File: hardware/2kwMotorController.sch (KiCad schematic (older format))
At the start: 0 parts

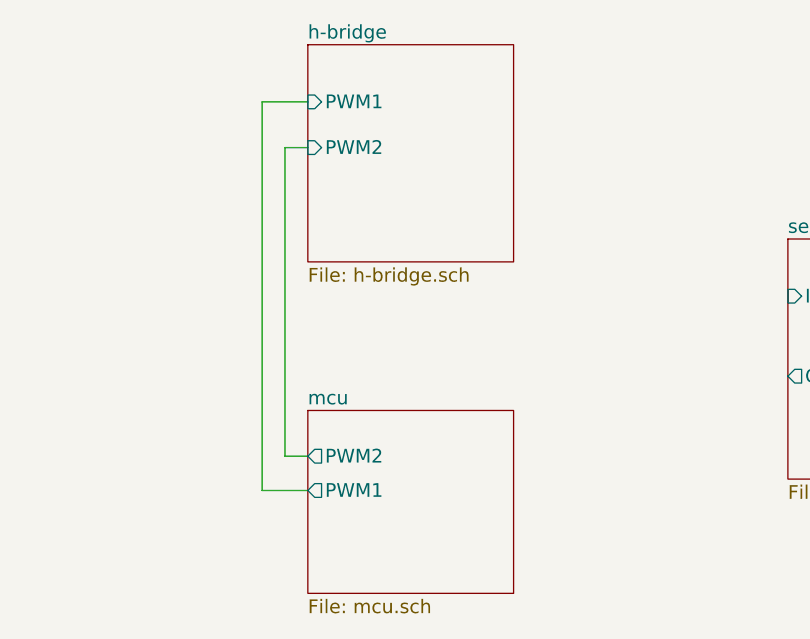
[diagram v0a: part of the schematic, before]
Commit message: cleaned up h-bridge; added digital isolators
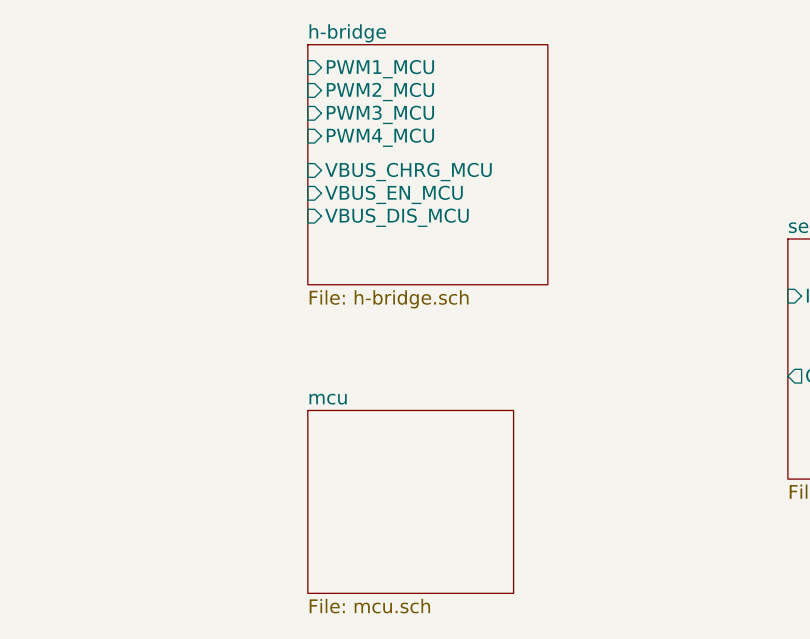
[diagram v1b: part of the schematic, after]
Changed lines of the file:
@@
 $EndDescr
 $Sheet
-S 5550 1950 900  950
+S 5550 1950 1050 1050
 U 5975734C
 F0 "h-bridge" 60
 F1 "h-bridge.sch" 60
-F2 "PWM1" I L 5550 2200 60
-F3 "PWM2" I L 5550 2400 60
+F2 "PWM1_MCU" I L 5550 2050 60
+F3 "PWM2_MCU" I L 5550 2150 60
+F4 "PWM3_MCU" I L 5550 2250 60
+F5 "PWM4_MCU" I L 5550 2350 60
+F6 "VBUS_CHRG_MCU" I L 5550 2500 60
+F7 "VBUS_EN_MCU" I L 5550 2600 60
+F8 "VBUS_DIS_MCU" I L 5550 2700 60
 $EndSheet
-$Sheet
-S 5550 3550 900  800
-U 59759ACE
-F0 "mcu" 60
-F1 "mcu.sch" 60
-F2 "PWM1" O L 5550 3900 60
-F3 "PWM2" O L 5550 3750 60
-$EndSheet
-Wire Wire Line
-	5550 2400 5450 2400
-Wire Wire Line
-	5450 2400 5450 3750
-Wire Wire Line
-	5450 3750 5550 3750
-Wire Wire Line
-	5550 3900 5350 3900
-Wire Wire Line
-	5350 3900 5350 2200
-Wire Wire Line
-	5350 2200 5550 2200
 $Sheet
 S 7650 2800 1200 1050
@@
 F1 "power.sch" 60
 $EndSheet
+$Sheet
+S 5550 3550 900  800
+U 59759ACE
+F0 "mcu" 60
+F1 "mcu.sch" 60
+$EndSheet
 $EndSCHEMATC

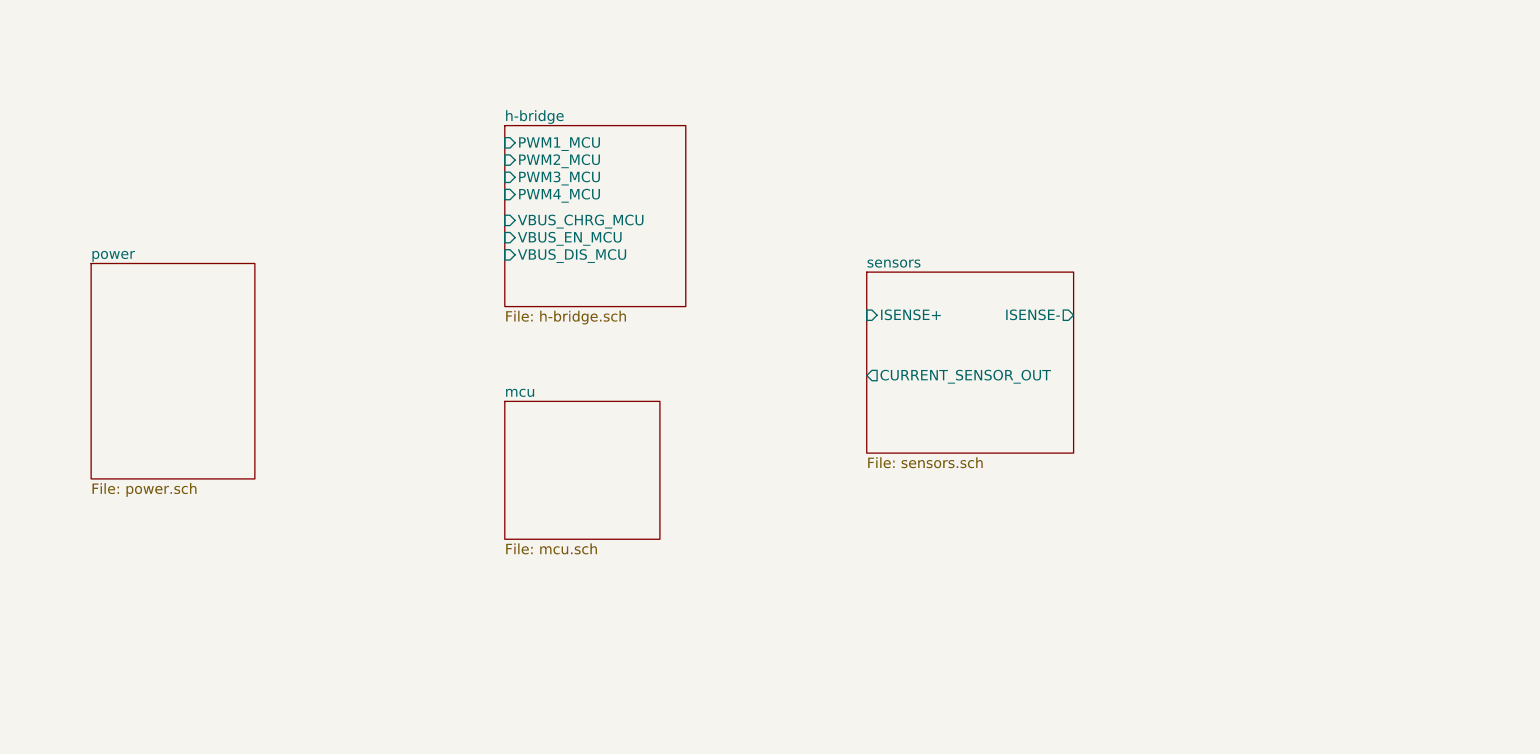
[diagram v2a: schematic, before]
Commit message: ERC cleanup, begin pcbnew population
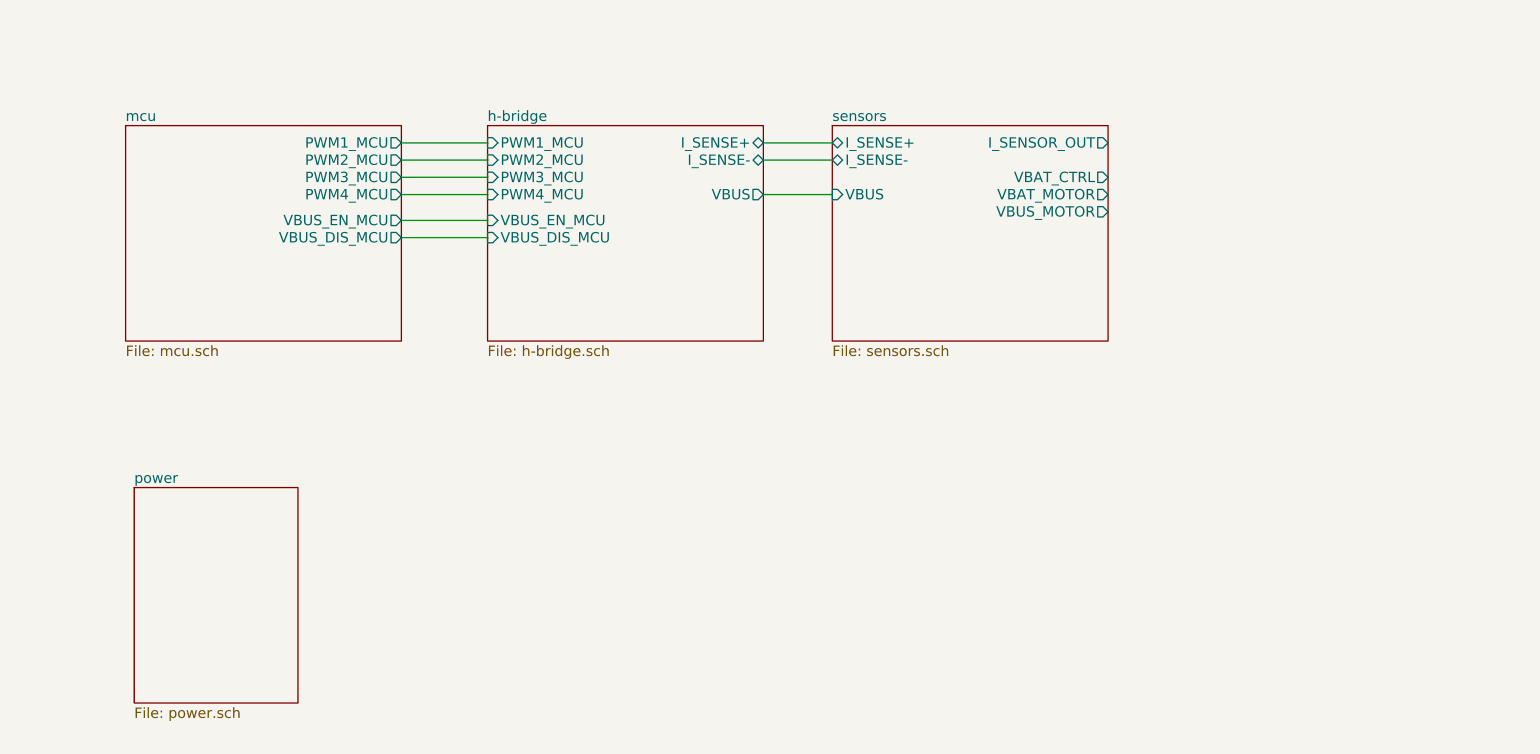
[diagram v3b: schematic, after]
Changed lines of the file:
@@
 $EndDescr
 $Sheet
-S 7650 2800 1200 1050
+S 7450 1950 1600 1250
 U 5975AD12
 F0 "sensors" 60
 F1 "sensors.sch" 60
-F2 "ISENSE+" I L 7650 3050 60
-F3 "ISENSE-" O R 8850 3050 60
-F4 "CURRENT_SENSOR_OUT" O L 7650 3400 60
+F2 "I_SENSE+" B L 7450 2050 60
+F3 "I_SENSE-" B L 7450 2150 60
+F4 "I_SENSOR_OUT" O R 9050 2050 60
+F5 "VBAT_CTRL" O R 9050 2250 60
+F6 "VBAT_MOTOR" O R 9050 2350 60
+F7 "VBUS_MOTOR" O R 9050 2450 60
+F8 "VBUS" I L 7450 2350 60
 $EndSheet
 $Sheet
-S 3150 2750 950  1250
+S 3400 4050 950  1250
 U 5975B0C1
 F0 "power" 60
@@
 $EndSheet
 $Sheet
-S 5550 3550 900  800
+S 3350 1950 1600 1250
 U 59759ACE
 F0 "mcu" 60
 F1 "mcu.sch" 60
+F2 "PWM1_MCU" O R 4950 2050 60
+F3 "PWM2_MCU" O R 4950 2150 60
+F4 "PWM3_MCU" O R 4950 2250 60
+F5 "PWM4_MCU" O R 4950 2350 60
+F6 "VBUS_EN_MCU" O R 4950 2500 60
+F7 "VBUS_DIS_MCU" O R 4950 2600 60
 $EndSheet
+Wire Wire Line
+	4950 2050 5450 2050
+Wire Wire Line
+	5450 2150 4950 2150
+Wire Wire Line
+	4950 2250 5450 2250
+Wire Wire Line
+	5450 2350 4950 2350
+Wire Wire Line
+	4950 2500 5450 2500
+Wire Wire Line
+	5450 2600 4950 2600
 $Sheet
-S 5550 1950 1050 1050
+S 5450 1950 1600 1250
 U 5975734C
 F0 "h-bridge" 60
 F1 "h-bridge.sch" 60
-F2 "PWM1_MCU" I L 5550 2050 60
-F3 "PWM2_MCU" I L 5550 2150 60
-F4 "PWM3_MCU" I L 5550 2250 60
-F5 "PWM4_MCU" I L 5550 2350 60
-F6 "VBUS_CHRG_MCU" I L 5550 2500 60
-F7 "VBUS_EN_MCU" I L 5550 2600 60
-F8 "VBUS_DIS_MCU" I L 5550 2700 60
+F2 "PWM1_MCU" I L 5450 2050 60
+F3 "PWM2_MCU" I L 5450 2150 60
+F4 "PWM3_MCU" I L 5450 2250 60
+F5 "PWM4_MCU" I L 5450 2350 60
+F6 "VBUS_EN_MCU" I L 5450 2500 60
+F7 "VBUS_DIS_MCU" I L 5450 2600 60
+F8 "I_SENSE+" B R 7050 2050 60
+F9 "I_SENSE-" B R 7050 2150 60
+F10 "VBUS" O R 7050 2350 60
 $EndSheet
+Wire Wire Line
+	7050 2050 7450 2050
+Wire Wire Line
+	7050 2150 7450 2150
+Wire Wire Line
+	7050 2350 7450 2350
 $EndSCHEMATC

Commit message: Finish MCU HW draft 1; adjust sensors for 3v ref
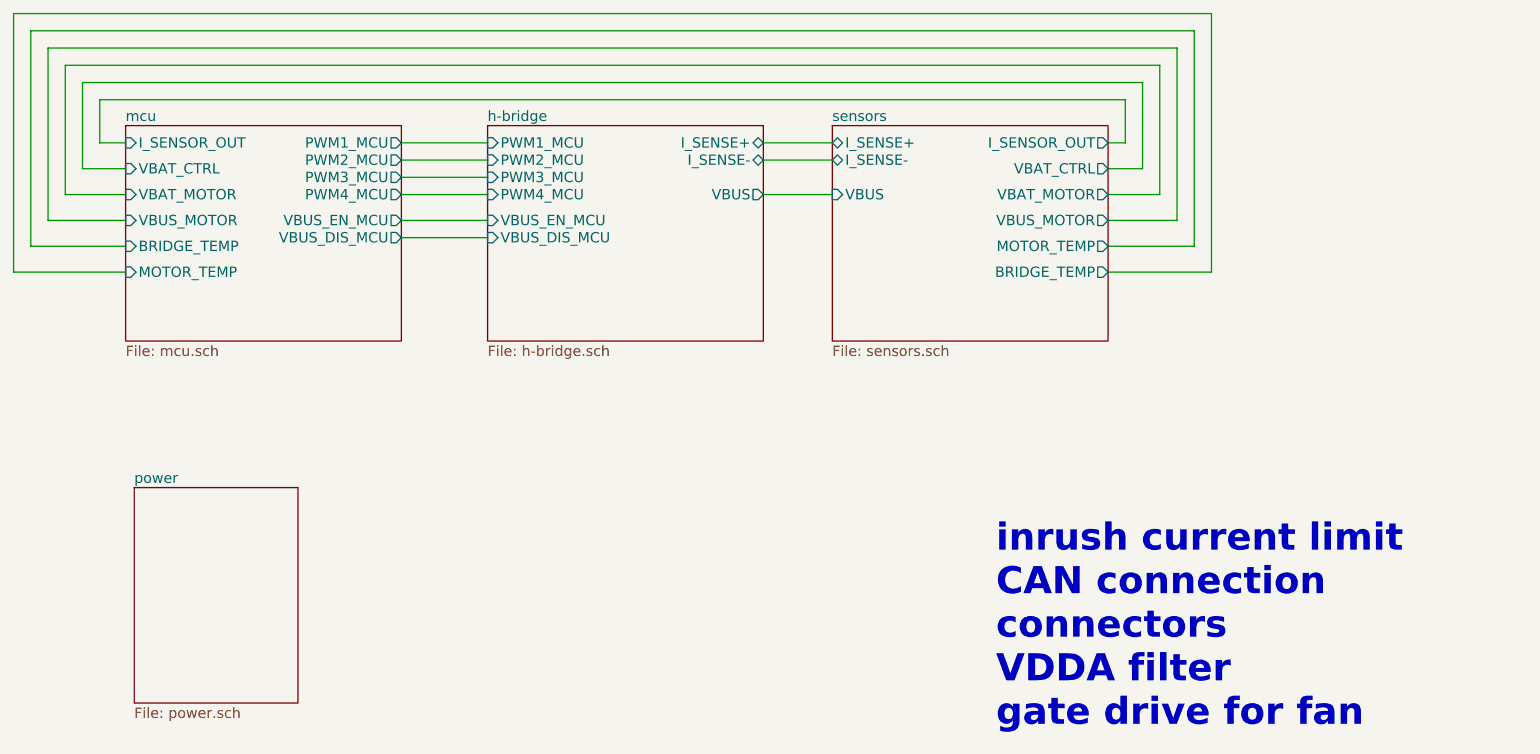
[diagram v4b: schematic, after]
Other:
- note added: "inrush current limit\nCAN connection\nconnectors\nVDDA filter\ngate drive for fan"
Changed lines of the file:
@@
 F3 "I_SENSE-" B L 7450 2150 60
 F4 "I_SENSOR_OUT" O R 9050 2050 60
-F5 "VBAT_CTRL" O R 9050 2250 60
+F5 "VBAT_CTRL" O R 9050 2200 60
 F6 "VBAT_MOTOR" O R 9050 2350 60
-F7 "VBUS_MOTOR" O R 9050 2450 60
+F7 "VBUS_MOTOR" O R 9050 2500 60
 F8 "VBUS" I L 7450 2350 60
+F9 "MOTOR_TEMP" O R 9050 2650 60
+F10 "BRIDGE_TEMP" O R 9050 2800 60
 $EndSheet
 $Sheet
@@
 F6 "VBUS_EN_MCU" O R 4950 2500 60
 F7 "VBUS_DIS_MCU" O R 4950 2600 60
+F8 "I_SENSOR_OUT" I L 3350 2050 60
+F9 "VBAT_CTRL" I L 3350 2200 60
+F10 "VBAT_MOTOR" I L 3350 2350 60
+F11 "VBUS_MOTOR" I L 3350 2500 60
+F12 "BRIDGE_TEMP" I L 3350 2650 60
+F13 "MOTOR_TEMP" I L 3350 2800 60
 $EndSheet
 Wire Wire Line
@@
 Wire Wire Line
 	7050 2350 7450 2350
+Wire Wire Line
+	9050 2050 9150 2050
+Wire Wire Line
+	9150 2050 9150 1800
+Wire Wire Line
+	9150 1800 3200 1800
+Wire Wire Line
+	9050 2200 9250 2200
+Wire Wire Line
+	9250 2200 9250 1700
+Wire Wire Line
+	9250 1700 3100 1700
+Wire Wire Line
+	3100 1700 3100 2200
+Wire Wire Line
+	3100 2200 3350 2200
+Wire Wire Line
+	3350 2050 3200 2050
+Wire Wire Line
+	3200 2050 3200 1800
+Wire Wire Line
+	3350 2350 3000 2350
+Wire Wire Line
+	3000 2350 3000 1600
+Wire Wire Line
+	3000 1600 9350 1600
+Wire Wire Line
+	9350 1600 9350 2350
+Wire Wire Line
+	9350 2350 9050 2350
+Wire Wire Line
+	9050 2500 9450 2500
+Wire Wire Line
+	9450 2500 9450 1500
+Wire Wire Line
+	9450 1500 2900 1500
+Wire Wire Line
+	2900 1500 2900 2500
+Wire Wire Line
+	2900 2500 3350 2500
+Wire Wire Line
+	3350 2650 2800 2650
+Wire Wire Line
+	2800 2650 2800 1400
+Wire Wire Line
+	2800 1400 9550 1400
+Wire Wire Line
+	9550 1400 9550 2650
+Wire Wire Line
+	9550 2650 9050 2650
+Wire Wire Line
+	9050 2800 9650 2800
+Wire Wire Line
+	9650 2800 9650 1300
+Wire Wire Line
+	9650 1300 2700 1300
+Wire Wire Line
+	2700 1300 2700 2800
+Wire Wire Line
+	2700 2800 3350 2800
+Text Notes 8400 5450 0    157  ~ 31
+inrush current limit\nCAN connection\nconnectors\nVDDA filter\ngate drive for fan
 $EndSCHEMATC

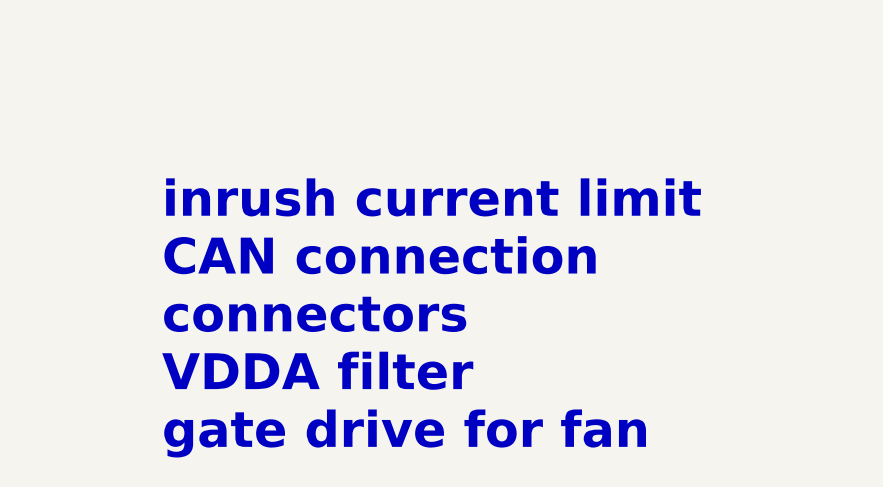
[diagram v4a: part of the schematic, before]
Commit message: Update sensors, hbridge caps, add heatsink
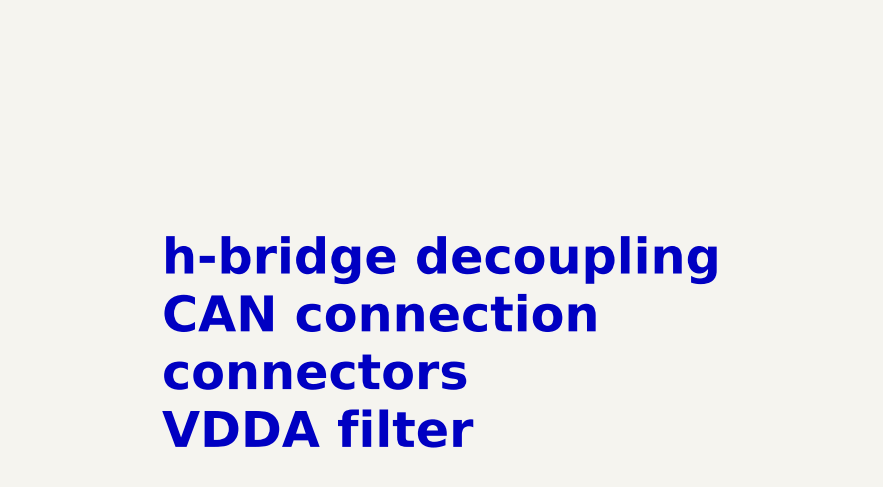
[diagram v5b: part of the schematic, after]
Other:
- note added: "h-bridge decoupling\nCAN connection\nconnectors\nVDDA filter"
- note removed: "inrush current limit\nCAN connection\nconnectors\nVDDA filter\ngate drive for fan"
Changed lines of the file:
@@
 	2700 2800 3350 2800
 Text Notes 8400 5450 0    157  ~ 31
-inrush current limit\nCAN connection\nconnectors\nVDDA filter\ngate drive for fan
+h-bridge decoupling\nCAN connection\nconnectors\nVDDA filter
 $EndSCHEMATC

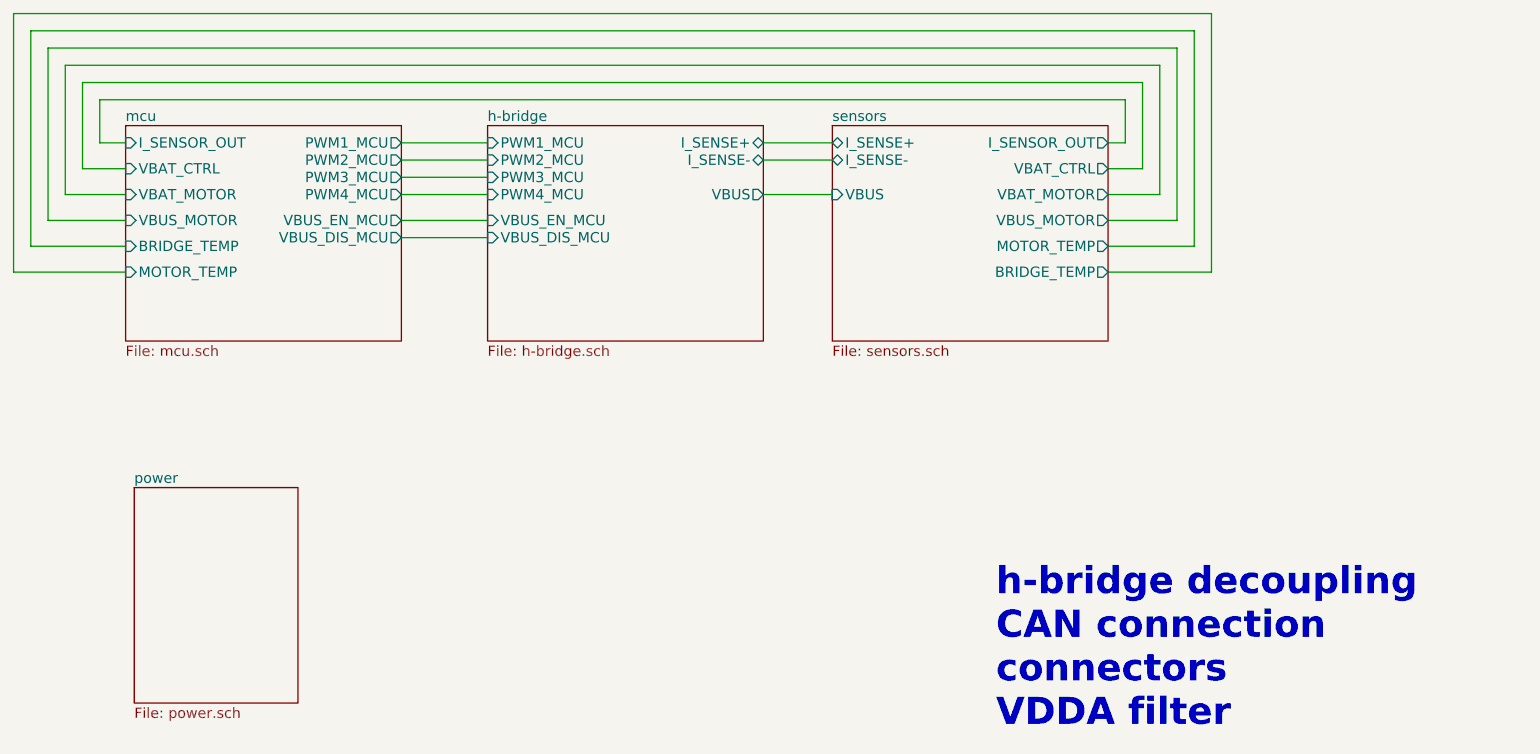
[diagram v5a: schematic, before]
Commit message: Draft layout of controller section
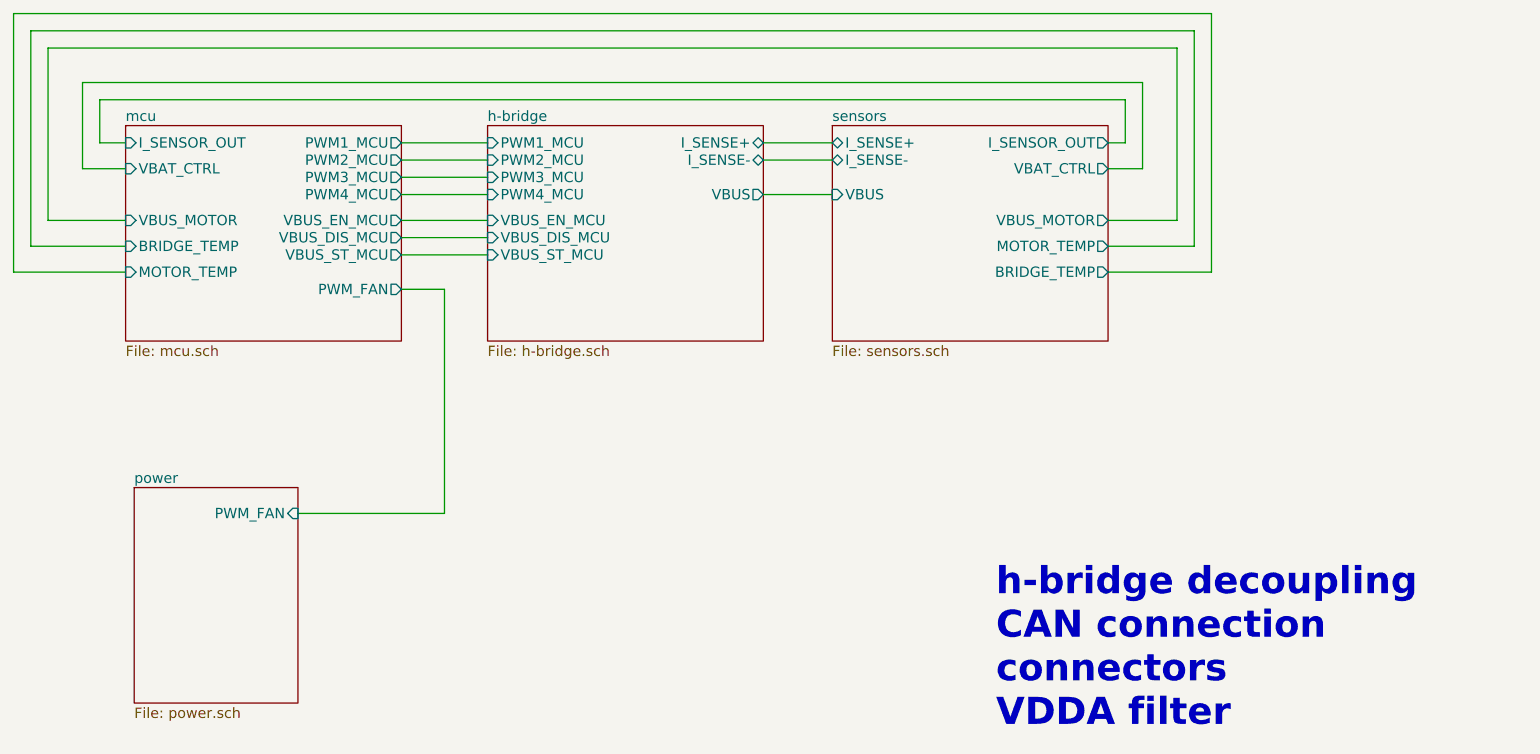
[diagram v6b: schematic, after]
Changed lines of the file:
@@
 F4 "I_SENSOR_OUT" O R 9050 2050 60
 F5 "VBAT_CTRL" O R 9050 2200 60
-F6 "VBAT_MOTOR" O R 9050 2350 60
-F7 "VBUS_MOTOR" O R 9050 2500 60
-F8 "VBUS" I L 7450 2350 60
-F9 "MOTOR_TEMP" O R 9050 2650 60
-F10 "BRIDGE_TEMP" O R 9050 2800 60
+F6 "VBUS_MOTOR" O R 9050 2500 60
+F7 "VBUS" I L 7450 2350 60
+F8 "MOTOR_TEMP" O R 9050 2650 60
+F9 "BRIDGE_TEMP" O R 9050 2800 60
 $EndSheet
 $Sheet
@@
 F0 "power" 60
 F1 "power.sch" 60
+F2 "PWM_FAN" I R 4350 4200 60
 $EndSheet
 $Sheet
@@
 F8 "I_SENSOR_OUT" I L 3350 2050 60
 F9 "VBAT_CTRL" I L 3350 2200 60
-F10 "VBAT_MOTOR" I L 3350 2350 60
-F11 "VBUS_MOTOR" I L 3350 2500 60
-F12 "BRIDGE_TEMP" I L 3350 2650 60
-F13 "MOTOR_TEMP" I L 3350 2800 60
+F10 "VBUS_MOTOR" I L 3350 2500 60
+F11 "BRIDGE_TEMP" I L 3350 2650 60
+F12 "MOTOR_TEMP" I L 3350 2800 60
+F13 "PWM_FAN" O R 4950 2900 60
+F14 "VBUS_ST_MCU" O R 4950 2700 60
 $EndSheet
 Wire Wire Line
@@
 F9 "I_SENSE-" B R 7050 2150 60
 F10 "VBUS" O R 7050 2350 60
+F11 "VBUS_ST_MCU" I L 5450 2700 60
 $EndSheet
 Wire Wire Line
@@
 Wire Wire Line
 	3200 2050 3200 1800
-Wire Wire Line
-	3350 2350 3000 2350
-Wire Wire Line
-	3000 2350 3000 1600
-Wire Wire Line
-	3000 1600 9350 1600
-Wire Wire Line
-	9350 1600 9350 2350
-Wire Wire Line
-	9350 2350 9050 2350
 Wire Wire Line
 	9050 2500 9450 2500
@@
 Text Notes 8400 5450 0    157  ~ 31
 h-bridge decoupling\nCAN connection\nconnectors\nVDDA filter
+Wire Wire Line
+	4950 2900 5200 2900
+Wire Wire Line
+	5200 2900 5200 4200
+Wire Wire Line
+	5200 4200 4350 4200
+Wire Wire Line
+	4950 2700 5450 2700
 $EndSCHEMATC
